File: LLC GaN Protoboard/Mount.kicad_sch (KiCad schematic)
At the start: 2 parts, among them J1 Conn_02x10_Top_Bottom, J2 Conn_02x10_Top_Bottom

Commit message: Initial layout
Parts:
- J1, J2: footprint (none) -> Connector_PinHeader_2.54mm:PinHeader_2x10_P2.54mm_Vertical
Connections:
- net PWM7A/HI: now reaches J2.1 (Pin_1)
- net GND: now reaches J2.11 (Pin_11)
- net GND: now also J1.12 (Pin_12)
- net LED: now reaches J2.18 (Pin_18)
- net PWM7B/LO: now reaches J2.2 (Pin_2)
- net ADCINA4/VIN: now reaches J1.16 (Pin_16)
- net ADCINB4/VOUT: now reaches J1.17 (Pin_17)
- net ADCINB5/IOUT: now reaches J1.18 (Pin_18)
- net ADCINA9/IIN: now reaches J1.6 (Pin_6)

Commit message: Finished schematic
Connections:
- net SPIB_PICO: now reaches J2.16 (Pin_16)
- net SPIB_POCI: now reaches J2.17 (Pin_17)
- net SPIB_CLK: now reaches J1.7 (Pin_7)
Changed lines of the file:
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@@
+		)
+	)
+	(hierarchical_label "SPIB_PICO"
+		(shape input)
+		(at 120.65 86.36 0)
+		(effects
+			(font
+				(size 1.27 1.27)
+			)
+			(justify left)
 		)
 	)
@@
 			)
 			(justify left)
+		)
+	)
+	(hierarchical_label "SPIB_CLK"
+		(shape input)
+		(at 72.39 88.9 180)
+		(effects
+			(font
+				(size 1.27 1.27)
+			)
+			(justify right)
 		)
 	)
@@
 		)
 	)
+	(hierarchical_label "SPIB_POCI"
+		(shape input)
+		(at 120.65 88.9 0)
+		(effects
+			(font
+				(size 1.27 1.27)
+			)
+			(justify left)
+		)
+	)

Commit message: Edited schematic
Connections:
- net SPIB_CLK: no longer names the net of J1.7 (Pin_7)
- net SPIB_PICO: no longer names the net of J2.16 (Pin_16)
- net SPIB_POCI: no longer names the net of J2.17 (Pin_17)
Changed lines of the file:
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@@
-		)
-	)
-	(hierarchical_label "SPIB_PICO"
-		(shape input)
-		(at 120.65 86.36 0)
-		(effects
-			(font
-				(size 1.27 1.27)
-			)
-			(justify left)
 		)
 	)
@@
 		)
 	)
-	(hierarchical_label "SPIB_CLK"
-		(shape input)
-		(at 72.39 88.9 180)
-		(effects
-			(font
-				(size 1.27 1.27)
-			)
-			(justify right)
-		)
-	)
 	(hierarchical_label "PWM7A{slash}HI"
 		(shape input)
@@
 		)
 	)
-	(hierarchical_label "SPIB_POCI"
-		(shape input)
-		(at 120.65 88.9 0)
-		(effects
-			(font
-				(size 1.27 1.27)
-			)
-			(justify left)
-		)
-	)
 	(hierarchical_label "ADCINB4{slash}VOUT"
 		(shape input)
 		(at 85.09 88.9 0)
-		(effects
-			(font
-				(size 1.27 1.27)
-			)
-			(justify left)
-		)
-	)
-	(hierarchical_label "+3.3V"
-		(shape input)
-		(at 72.39 73.66 180)
-		(effects
-			(font
-				(size 1.27 1.27)
-			)
-			(justify right)
-		)
-	)
-	(hierarchical_label "+5V"
-		(shape input)
-		(at 85.09 73.66 0)
 		(effects
 			(font
@@
 	)
 	(symbol
+		(lib_id "power:+5V")
+		(at 85.09 73.66 270)
+		(unit 1)
+		(body_style 1)
+		(exclude_from_sim no)
+		(in_bom yes)
+		(on_board yes)
+		(in_pos_files yes)
+		(dnp no)
+		(fields_autoplaced yes)
+		(property "Reference" "#PWR042"
+			(at 81.28 73.66 0)
+			(hide yes)
+			(show_name no)
+			(do_not_autoplace no)
+			(effects
+				(font
+					(size 1.27 1.27)
+				)
+			)
+		)
+		(property "Value" "+5V"
+			(at 88.9 73.6599 90)
+			(show_name no)
+			(do_not_autoplace no)
+			(effects
+				(font
+					(size 1.27 1.27)
+				)
+				(justify left)
+			)
+		)
+		(property "Footprint" ""
+			(at 85.09 73.66 0)
+			(hide yes)
+			(show_name no)
+			(do_not_autoplace no)
+			(effects
+				(font
+					(size 1.27 1.27)
+				)
+			)
+		)
+		(property "Datasheet" ""
+			(at 85.09 73.66 0)
+			(hide yes)
+			(show_name no)
+			(do_not_autoplace no)
+			(effects
+				(font
+					(size 1.27 1.27)
+				)
+			)
+		)
+		(property "Description" "Power symbol creates a global label with name \"+5V\""
+			(at 85.09 73.66 0)
+			(hide yes)
+			(show_name no)
+			(do_not_autoplace no)
+			(effects
+				(font
+					(size 1.27 1.27)
+				)
+			)
+		)
+		(pin "1"
+		)
+		(instances
+			(project "LLC GaN Protoboard"
+				(path "/07813ae8-ed9f-4173-b5dd-dce781eafd3c/a27e07b3-6ec1-4c0c-a63f-5e7408c5e375"
+					(reference "#PWR042")
+					(unit 1)
+				)
+			)
+		)
+	)
+	(symbol
 		(lib_id "Connector_Generic:Conn_02x10_Top_Bottom")
 		(at 77.47 83.82 0)
@@
 					(unit 1)
 				)
+			)
+		)
+	)
+	(symbol
+		(lib_id "power:+3.3V")
+		(at 72.39 73.66 90)
+		(unit 1)
+		(body_style 1)
+		(exclude_from_sim no)
+		(in_bom yes)
+		(on_board yes)
+		(in_pos_files yes)
+		(dnp no)
+		(fields_autoplaced yes)
+		(property "Reference" "#PWR043"
+			(at 76.2 73.66 0)
+			(hide yes)
+			(show_name no)
+			(do_not_autoplace no)
+			(effects
+				(font
+					(size 1.27 1.27)
+				)
+			)
+		)
+		(property "Value" "+3.3V"
+			(at 68.58 73.6599 90)
+			(show_name no)
+			(do_not_autoplace no)
+			(effects
+				(font
+					(size 1.27 1.27)
+				)
+				(justify left)
+			)
+		)
+		(property "Footprint" ""
+			(at 72.39 73.66 0)
+			(hide yes)
+			(show_name no)
+			(do_not_autoplace no)
+			(effects
+				(font
+					(size 1.27 1.27)
+				)
+			)
+		)
+		(property "Datasheet" ""
+			(at 72.39 73.66 0)
+			(hide yes)
+			(show_name no)
+			(do_not_autoplace no)
+			(effects
+				(font
+					(size 1.27 1.27)
+				)
+			)
+		)
+		(property "Description" "Power symbol creates a global label with name \"+3.3V\""
+			(at 72.39 73.66 0)
+			(hide yes)
+			(show_name no)
+			(do_not_autoplace no)
+			(effects
+				(font
+					(size 1.27 1.27)
+				)
+			)
+		)
+		(pin "1"
+		)
+		(instances
+			(project "LLC GaN Protoboard"
+				(path "/07813ae8-ed9f-4173-b5dd-dce781eafd3c/a27e07b3-6ec1-4c0c-a63f-5e7408c5e375"
+					(reference "#PWR043")
+					(unit 1)
+				)

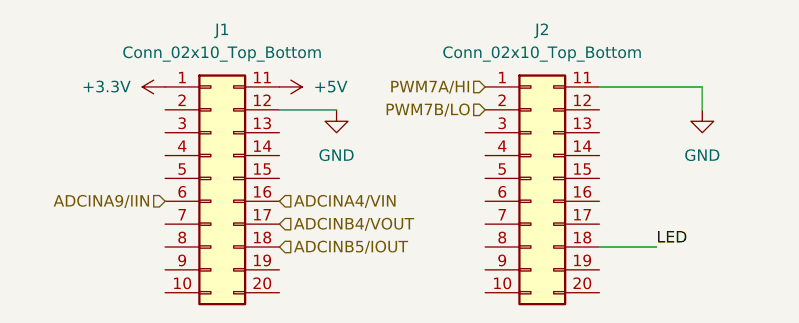
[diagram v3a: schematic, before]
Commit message: Initial primary side layout
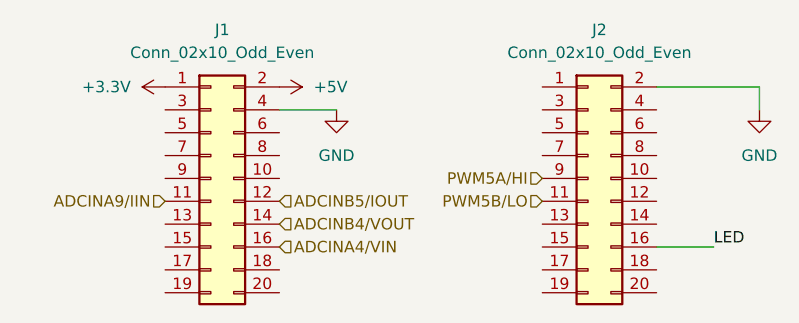
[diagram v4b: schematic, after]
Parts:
- removed J1, J2: Conn_02x10_Top_Bottom, Connector_PinHeader_2.54mm:PinHeader_2x10_P2.54mm_Vertical, symbol Connector_Generic:Conn_02x10_Top_Bottom
- added J1, J2: Conn_02x10_Odd_Even, Connector_PinSocket_2.54mm:PinSocket_2x10_P2.54mm_Vertical, symbol Connector_Generic:Conn_02x10_Odd_Even
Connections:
- net +3.3V: now also J1.1 (Pin_1)
- net +5V: now also J1.2 (Pin_2)
- net ADCINA4/VIN: now also J1.16 (Pin_16)
- net ADCINA9/IIN: now also J1.11 (Pin_11)
- net ADCINB4/VOUT: now also J1.14 (Pin_14)
- net ADCINB5/IOUT: now also J1.12 (Pin_12)
- net GND: now also J1.4 (Pin_4), J2.2 (Pin_2)
- net LED: now also J2.16 (Pin_16)
- new net PWM5A/HI: J2.9 (Pin_9)
- new net PWM5B/LO: J2.11 (Pin_11)
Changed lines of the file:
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@@
 	(wire
 		(pts
-			(xy 132.08 73.66) (xy 132.08 76.2)
+			(xy 138.43 73.66) (xy 138.43 76.2)
 		)
 		(stroke
@@
 	(wire
 		(pts
-			(xy 120.65 73.66) (xy 132.08 73.66)
+			(xy 127 73.66) (xy 138.43 73.66)
 		)
 		(stroke
@@
 	(wire
 		(pts
-			(xy 127 91.44) (xy 120.65 91.44)
+			(xy 133.35 91.44) (xy 127 91.44)
 		)
 		(stroke
@@
 	)
 	(label "LED"
-		(at 127 91.44 0)
+		(at 133.35 91.44 0)
 		(effects
 			(font
@@
 		)
 	)
-	(hierarchical_label "ADCINA4{slash}VIN"
+	(hierarchical_label "ADCINB4{slash}VOUT"
+		(shape input)
+		(at 85.09 88.9 0)
+		(effects
+			(font
+				(size 1.27 1.27)
+			)
+			(justify left)
+		)
+	)
+	(hierarchical_label "ADCINB5{slash}IOUT"
 		(shape input)
 		(at 85.09 86.36 0)
@@
 		)
 	)
-	(hierarchical_label "PWM7A{slash}HI"
+	(hierarchical_label "ADCINA4{slash}VIN"
 		(shape input)
-		(at 107.95 73.66 180)
+		(at 85.09 91.44 0)
 		(effects
 			(font
 				(size 1.27 1.27)
 			)
-			(justify right)
+			(justify left)
 		)
 	)
@@
 		)
 	)
-	(hierarchical_label "ADCINB4{slash}VOUT"
+	(hierarchical_label "PWM5A{slash}HI"
 		(shape input)
-		(at 85.09 88.9 0)
+		(at 114.3 83.82 180)
 		(effects
 			(font
 				(size 1.27 1.27)
 			)
-			(justify left)
-		)
-	)
-	(hierarchical_label "ADCINB5{slash}IOUT"
+			(justify right)
+		)
+	)
+	(hierarchical_label "PWM5B{slash}LO"
 		(shape input)
-		(at 85.09 91.44 0)
-		(effects
-			(font
-				(size 1.27 1.27)
-			)
-			(justify left)
-		)
-	)
-	(hierarchical_label "PWM7B{slash}LO"
-		(shape input)
-		(at 107.95 76.2 180)
+		(at 114.3 86.36 180)
 		(effects
 			(font
@@
 	)
 	(symbol
-		(lib_id "Connector_Generic:Conn_02x10_Top_Bottom")
-		(at 113.03 83.82 0)
-		(unit 1)
-		(body_style 1)
-		(exclude_from_sim no)
-		(in_bom yes)
-		(on_board yes)
-		(in_pos_files yes)
-		(dnp no)
-		(fields_autoplaced yes)
-		(property "Reference" "J2"
-			(at 114.3 67.31 0)
-			(show_name no)
-			(do_not_autoplace no)
-			(effects
-				(font
-					(size 1.27 1.27)
-				)
-			)
-		)
-		(property "Value" "Conn_02x10_Top_Bottom"
-			(at 114.3 69.85 0)
-			(show_name no)
-			(do_not_autoplace no)
-			(effects
-				(font
-					(size 1.27 1.27)
-				)
-			)
-		)
-		(property "Footprint" "Connector_PinHeader_2.54mm:PinHeader_2x10_P2.54mm_Vertical"
-			(at 113.03 83.82 0)
-			(hide yes)
-			(show_name no)
-			(do_not_autoplace no)
-			(effects
-				(font
-					(size 1.27 1.27)
-				)
-			)
-		)
-		(property "Datasheet" ""
-			(at 113.03 83.82 0)
-			(hide yes)
-			(show_name no)
-			(do_not_autoplace no)
-			(effects
-				(font
-					(size 1.27 1.27)
-				)
-			)
-		)
-		(property "Description" "Generic connector, double row, 02x10, top/bottom pin numbering scheme (row 1: 1...pins_per_row, row2: pins_per_row+1 ... num_pins), script generated (kicad-library-utils/schlib/autogen/connector/)"
-			(at 113.03 83.82 0)
-			(hide yes)
-			(show_name no)
-			(do_not_autoplace no)
-			(effects
-				(font
-					(size 1.27 1.27)
-				)
-			)
-		)
-		(pin "2"
-		)
-		(pin "10"
-		)
-		(pin "3"
-		)
-		(pin "11"
-		)
-		(pin "8"
-		)
-		(pin "12"
-		)
-		(pin "13"
-		)
-		(pin "9"
-		)
-		(pin "14"
-		)
-		(pin "15"
-		)
-		(pin "6"
-		)
-		(pin "5"
-		)
-		(pin "4"
-		)
-		(pin "7"
-		)
-		(pin "1"
-		)
-		(pin "20"
-		)
-		(pin "16"
-		)
-		(pin "17"
-		)
-		(pin "18"
-		)
-		(pin "19"
-		)
-		(instances
-			(project "LLC GaN Protoboard"
-				(path "/07813ae8-ed9f-4173-b5dd-dce781eafd3c/a27e07b3-6ec1-4c0c-a63f-5e7408c5e375"
-					(reference "J2")
-					(unit 1)
-				)
-			)
-		)
-	)
-	(symbol
 		(lib_id "power:GND")
-		(at 132.08 76.2 0)
+		(at 138.43 76.2 0)
 		(unit 1)
 		(body_style 1)
@@
 		(fields_autoplaced yes)
 		(property "Reference" "#PWR09"
-			(at 132.08 82.55 0)
+			(at 138.43 82.55 0)
 			(hide yes)
 			(show_name no)
@@
 		)
 		(property "Value" "GND"
-			(at 132.08 81.28 0)
+			(at 138.43 81.28 0)
 			(show_name no)
 			(do_not_autoplace no)
@@
 		)
 		(property "Footprint" ""
-			(at 132.08 76.2 0)
+			(at 138.43 76.2 0)
 			(hide yes)
 			(show_name no)
@@
 		)
 		(property "Datasheet" ""
-			(at 132.08 76.2 0)
+			(at 138.43 76.2 0)
 			(hide yes)
 			(show_name no)
@@
 		)
 		(property "Description" "Power symbol creates a global label with name \"GND\" , ground"
-			(at 132.08 76.2 0)
+			(at 138.43 76.2 0)
 			(hide yes)
 			(show_name no)
@@
 	)
 	(symbol
-		(lib_id "Connector_Generic:Conn_02x10_Top_Bottom")
+		(lib_id "Connector_Generic:Conn_02x10_Odd_Even")
 		(at 77.47 83.82 0)
 		(unit 1)
@@
 			)
 		)
-		(property "Value" "Conn_02x10_Top_Bottom"
+		(property "Value" "Conn_02x10_Odd_Even"
 			(at 78.74 69.85 0)
 			(show_name no)
@@
 			)
 		)
-		(property "Footprint" "Connector_PinHeader_2.54mm:PinHeader_2x10_P2.54mm_Vertical"
+		(property "Footprint" "Connector_PinSocket_2.54mm:PinSocket_2x10_P2.54mm_Vertical"
 			(at 77.47 83.82 0)
 			(hide yes)
@@
 			)
 		)
-		(property "Description" "Generic connector, double row, 02x10, top/bottom pin numbering scheme (row 1: 1...pins_per_row, row2: pins_per_row+1 ... num_pins), script generated (kicad-library-utils/schlib/autogen/connector/)"
+		(property "Description" "Generic connector, double row, 02x10, odd/even pin numbering scheme (row 1 odd numbers, row 2 even numbers), script generated (kicad-library-utils/schlib/autogen/connector/)"
 			(at 77.47 83.82 0)
 			(hide yes)
@@
 			)
 		)
+		(pin "11"
+		)
+		(pin "14"
+		)
+		(pin "13"
+		)
 		(pin "8"
 		)
+		(pin "3"
+		)
+		(pin "9"
+		)
+		(pin "2"
+		)
+		(pin "18"
+		)
+		(pin "6"
+		)
+		(pin "16"
+		)
+		(pin "5"
+		)
+		(pin "20"
+		)
+		(pin "1"
+		)
+		(pin "19"
+		)
+		(pin "15"
+		)
 		(pin "7"
 		)
+		(pin "10"
+		)
 		(pin "17"
 		)
-		(pin "19"
-		)
-		(pin "15"
-		)
 		(pin "4"
 		)
-		(pin "9"
-		)
-		(pin "6"
-		)
-		(pin "10"
-		)
-		(pin "13"
-		)
-		(pin "14"
-		)
-		(pin "18"
-		)
-		(pin "5"
-		)
-		(pin "1"
-		)
-		(pin "11"
-		)
-		(pin "20"
-		)
-		(pin "2"
-		)
 		(pin "12"
-		)
-		(pin "3"
-		)
-		(pin "16"
 		)
 		(instances
@@
 					(unit 1)
 				)
+			)
+		)
+	)
+	(symbol
+		(lib_id "Connector_Generic:Conn_02x10_Odd_Even")
+		(at 119.38 83.82 0)
+		(unit 1)
+		(body_style 1)
+		(exclude_from_sim no)
+		(in_bom yes)
+		(on_board yes)
+		(in_pos_files yes)
+		(dnp no)
+		(fields_autoplaced yes)
+		(property "Reference" "J2"
+			(at 120.65 67.31 0)
+			(show_name no)
+			(do_not_autoplace no)
+			(effects
+				(font
+					(size 1.27 1.27)
+				)
+			)
+		)
+		(property "Value" "Conn_02x10_Odd_Even"
+			(at 120.65 69.85 0)
+			(show_name no)
+			(do_not_autoplace no)
+			(effects
+				(font
+					(size 1.27 1.27)
+				)
+			)
+		)
+		(property "Footprint" "Connector_PinSocket_2.54mm:PinSocket_2x10_P2.54mm_Vertical"
+			(at 119.38 83.82 0)
+			(hide yes)
+			(show_name no)
+			(do_not_autoplace no)
+			(effects
+				(font
+					(size 1.27 1.27)
+				)
+			)
+		)
+		(property "Datasheet" ""
+			(at 119.38 83.82 0)
+			(hide yes)
+			(show_name no)
+			(do_not_autoplace no)
+			(effects
+				(font
+					(size 1.27 1.27)
+				)
+			)
+		)
+		(property "Description" "Generic connector, double row, 02x10, odd/even pin numbering scheme (row 1 odd numbers, row 2 even numbers), script generated (kicad-library-utils/schlib/autogen/connector/)"
+			(at 119.38 83.82 0)
+			(hide yes)
+			(show_name no)
+			(do_not_autoplace no)
+			(effects
+				(font
+					(size 1.27 1.27)
+				)
+			)
+		)
+		(pin "11"
+		)
+		(pin "14"
+		)
+		(pin "13"
+		)
+		(pin "8"
+		)
+		(pin "3"
+		)
+		(pin "9"
+		)
+		(pin "2"
+		)
+		(pin "18"
+		)
+		(pin "6"
+		)
+		(pin "16"
+		)
+		(pin "5"
+		)
+		(pin "20"
+		)
+		(pin "1"
+		)
+		(pin "19"
+		)
+		(pin "15"
+		)
+		(pin "7"
+		)
+		(pin "10"
+		)
+		(pin "17"
+		)
+		(pin "4"
+		)
+		(pin "12"
+		)
+		(instances
+			(project "LLC GaN Protoboard"
+				(path "/07813ae8-ed9f-4173-b5dd-dce781eafd3c/a27e07b3-6ec1-4c0c-a63f-5e7408c5e375"
+					(reference "J2")
+					(unit 1)
+				)
